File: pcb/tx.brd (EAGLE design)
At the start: 30 x 40 mm, 9 parts

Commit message: dt rx done
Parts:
- added BT1: (no value), SparkFun-Batteries:BATTCON_24.5MM_PTH
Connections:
- new net +: BT1.3
- new net -: BT1.2
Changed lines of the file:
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@@
 <?xml version="1.0" encoding="utf-8"?>
 <!DOCTYPE eagle SYSTEM "eagle.dtd">
-<eagle version="9.1.0">
+<eagle version="9.1.3">
 <drawing>
 <settings>
-<setting alwaysvectorfont="no"/>
+<setting alwaysvectorfont="yes"/>
 <setting verticaltext="up"/>
 </settings>
@@
 <element name="U$7" library="L1" package="M3_MOUNTING_HOLE_PACK" value="M3_MOUNTING_HOLE" x="2.54" y="2.54"/>
 <element name="U$8" library="L1" package="M3_MOUNTING_HOLE_PACK" value="M3_MOUNTING_HOLE" x="27.94" y="2.54"/>
+<element name="BT1" library="SparkFun-Batteries" package="BATTCON_24.5MM_PTH" value="" x="15.24" y="-12.7">
+<attribute name="SF_SKU" value="PRT-08863" x="15.24" y="-12.7" size="1.778" layer="27" display="off"/>
+</element>
 </elements>
 <signals>
@@
 <wire x1="14.2537" y1="29.8654" x2="15.7331" y2="29.8654" width="0" layer="19" extent="1-1"/>
 </signal>
+<signal name="-">
+<contactref element="BT1" pad="2"/>
+</signal>
+<signal name="+">
+<contactref element="BT1" pad="3"/>
+</signal>
 </signals>

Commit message: before tx firmware test
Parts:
- added C1, C3: 100nF, clock:0805
- added C10: 4.7µF, SparkFun-Passives:0805
- added C11, C12: 4.7uF, clock:0805
- added C2, C6: 2.2nF, clock:0805
- added C4: 1.5pF, clock:0805
- added C5: 1pF, clock:0805
- added C7: 4.7pF, clock:0805
- added C8, C9: 22pF, clock:0805
- added D1, D2: BAT20J, SparkFun-DiscreteSemi:SOD-323
- added L1: 3.9nH, basicBoard:0805
- added L2: 8.2nH, basicBoard:0805
- added L3: 2.7nH, basicBoard:0805
- added LED1: (no value), joyAnalog:CHIP-LED0805
- added R1: 22K, joyAnalog:0805
- added R2, R3: 5K1, joyAnalog:0805
- added R4: 4.7K, SparkFun-Passives:0805
- added R5: 27K, SparkFun-Passives:0805
- added S2: (no value), Adafruit Feather M0 Adalogger:SWITCH-SPST-SMD-A
- added U$9: XC6206_DEV, 3pos_slide_switch:SOT23R_INFINEON
- added U3: MCP73831T-2ACI/OT, microbuilder:SOT23-5
- added Y1: CRYSTAL-26MHZSMD-3.2X2.5, SparkFun-Clocks:CRYSTAL-SMD-3.2X2.5MM
- BT1: device SparkFun-Batteries:BATTCON_24.5MM_PTH -> tx:TX_SPARKFUN-BATTERIES_BATTCON_24.5MM_PTH
- U$1: value USBC_6P_DEV -> L1_USBC_6P_DEV; device L1:USBC_6P_PAC -> tx:L1_USBC_6P_PAC
- moved BT1 29.0 mm to (14.0, 16.3), flipped to the bottom, turned to 180 degrees
- moved U$6 5.60 mm to (26.4, 34.8)
- moved U$5 5.21 mm to (2.54, 34.4)
- moved U$4 5.00 mm to (10.3, 40.4)
- moved U$1 3.32 mm to (14.0, 3.30)
- moved U$3 2.18 mm to (13.5, 26.7), turned to 90 degrees
- moved U$2 1.93 mm to (14.5, 14.5), turned to 180 degrees
- moved U1 1.82 mm to (14.0, 21.5)
- moved U$8 1.80 mm to (26.1, 2.54)
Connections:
- removed net +: BT1.3
- removed net -: BT1.2
- removed net DVDD: U$3.19
- removed net VDD: U$3.15, U$3.18, U$3.7
- removed net VDD_PA: U$3.11
- removed net VSS: U$3.0, U$3.14, U$3.17, U$3.20, U$3.8
- new net +3V3: C1.1, C12.1, C2.1, U$3.15, U$3.18, U$3.7, U$9.2
- new net N$1: C3.1, U$3.19
- new net N$10: R3.1, U$1.CC2
- new net N$11: R2.1, U$1.CC1
- new net N$12: LED1.C, R4.1
- new net N$13: R4.2, U3.1
- new net N$14: U$3.4
- new net N$15: U$3.5
- new net N$16: U$3.3
- new net N$17: R5.1, U3.5
- new net N$19: D2.A, S2.2
- new net N$2: R1.1, U$3.16
- new net N$20: U$3.2
- new net N$21: U$3.1
- new net N$25: BT1.1, C10.1, S2.3, U3.3
- new net N$26: D1.A, U$1.VBUS1, U$1.VBUS2
- new net N$27: C11.1, D1.C, D2.C, LED1.A, U$9.3, U3.4
- new net N$3: L1.1, L2.1, U$3.13
- new net N$4: C4.1, L1.2
- new net N$5: C4.2, C5.1
- new net N$6: L2.2, L3.1, U$3.12
- new net N$7: C8.1, U$3.9, Y1.1
- new net N$8: C6.1, C7.1, L3.2, U$3.11
- new net N$9: C9.1, U$3.10, Y1.3
- net GND: now also BT1.2, C1.2, C10.2, C11.2, C12.2, C2.2, C3.2, C5.2, C6.2, C7.2, C8.2, C9.2, R1.2, R2.2, R3.2, R5.2, U$1.1, U$1.2, U$1.3, U$1.4, U$1.GND1, U$1.GND2, U$3.0, U$3.14, U$3.17, U$3.20, U$3.8, U$9.1, U3.2, Y1.2, Y1.4
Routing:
- added copper zone on layer 1, net GND
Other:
- board size 30 x 40 mm -> 28.1 x 45 mm

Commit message: tx before cleanup
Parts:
- added 4K7, R9: 22K, joyAnalog:0805
- added C13: 100nF, clock:0805
- added C14, C15: 4.7uF, clock:0805
- added JP1: (no value), adafruit_changed:1X03-CLEANBIG
- added LED2: (no value), joyAnalog:CHIP-LED0805
- added R10, R11: 100K, SparkFun-Passives:0805
- added R6, R7, R8: 27K, SparkFun-Passives:0805
- added U$10: 324_SW, 3pos_slide_switch:342_SWICH_FOOT
- added U$11: PINHD1X2, adafruit_changed:1X02
- S2: device Adafruit Feather M0 Adalogger:SWITCH-SPST-SMD-A -> tx:SWITCH-SPST-SMD-A
- moved C10 17.9 mm to (5.71, 1.65), turned to 270 degrees
- moved R2 11.6 mm to (24.6, 5.89), turned to 90 degrees
- moved U1 8.79 mm to (13.2, 12.8), turned to 270 degrees
- moved C1 7.66 mm to (8.20, 19.2)
- moved C2 7.66 mm to (8.20, 20.7)
- moved C3 7.66 mm to (8.20, 17.6)
- moved R1 7.66 mm to (8.20, 22.2)
- moved U$4 7.53 mm to (9.85, 32.9)
- moved C9 7.41 mm to (17.4, 23.1)
- moved Y1 7.37 mm to (17.4, 20.1)
- moved U$6 7.36 mm to (25.5, 27.5)
- moved U$3 7.22 mm to (12.8, 19.5)
- moved L2 7.20 mm to (13.1, 22.9)
- moved L1 7.19 mm to (12.4, 25.2)
- moved L3 7.19 mm to (14.0, 25.2)
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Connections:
- removed net AVDD: U1.11
- removed net AVDDVCSEL: U1.1
- removed net AVSSVCSEL: U1.2
- new net N$18: R6.1, U$2.18, U1.9
- new net N$22: R7.1, U$2.17, U1.10
- new net N$23: R8.1, U$2.2, U1.5
- new net N$24: U$2.3, U1.7
- new net N$28: 4K7.2, LED2.C
- new net N$29: LED2.A, U$2.7
- new net N$30: U$10.P$2, U$2.10
- new net N$31: JP1.3, U$2.19
- new net N$32: JP1.2, U$2.20
- new net N$33: JP1.1, U$2.8
- new net N$35: R10.1, R11.2, U$2.9
- net +3V3: now also C13.1, C14.1, C15.1, R6.2, R7.2, U$11.1, U$2.16, U$2.5, U1.1, U1.11
- net GND: now also 4K7.1, C13.2, C14.2, C15.2, R11.1, R8.2, R9.2, S2.G1, S2.G2, S2.G3, S2.G4, U$10.P$4, U$11.2, U$2.1, U$2.15, U$4.GND, U$4.GND@1, U1.2
- net N$14: now also U$2.13
- net N$15: now also U$2.12
- net N$16: now also U$2.11
- net N$20: now also U$2.14
- net N$21: now also R9.1, U$2.6
- net N$27: now also R10.2
- net N$5: now also U$4.FEED
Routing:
- net +3V3: track 0.00 -> 34.2 mm, vias 0 -> 8
- net N$35: track 0.00 -> 31.2 mm, vias 0 -> 2
- net N$30: track 0.00 -> 29.0 mm, vias 0 -> 2
- net GND: track 0.00 -> 26.1 mm
- net N$29: track 0.00 -> 25.9 mm, vias 0 -> 2
- net N$27: track 0.00 -> 21.3 mm
- net N$25: track 0.00 -> 21.2 mm
- net N$21: track 0.00 -> 20.9 mm, vias 0 -> 2
- net N$26: track 0.00 -> 18.1 mm
- net N$23: track 0.00 -> 13.9 mm, vias 0 -> 2
- net N$16: track 0.00 -> 13.4 mm, vias 0 -> 2
- net N$32: track 0.00 -> 13.3 mm, vias 0 -> 1
- net N$20: track 0.00 -> 12.5 mm
- net N$24: track 0.00 -> 11.6 mm, vias 0 -> 2
- net N$14: track 0.00 -> 10.6 mm
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- added copper zone on layer 16, net +3V3
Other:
- board size 28.1 x 45 mm -> 28 x 37 mm

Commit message: tx almost done
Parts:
- removed 4K7: 22K, joyAnalog:0805
- added R12: 4K7, joyAnalog:0805
- C14, C15: value 4.7uF -> 100nF
- R6, R7, R8: value 27K -> 10K
- R9: value 22K -> 10K
- moved U$10 2.39 mm to (1.68, 21.8)
- moved R8 0.94 mm to (11.6, 13.7)
- moved U1 0.86 mm to (14.0, 13.0)
- moved C13 0.76 mm to (13.9, 9.35)
- moved U$11 0.76 mm to (26.7, 23.4)
- moved JP1 0.71 mm to (26.7, 9.91)
- moved R6 0.69 mm to (16.4, 13.9)
- moved R7 0.66 mm to (16.4, 11.0)
- moved U$9 0.63 mm to (6.71, 14.9)
- moved C11 0.40 mm to (4.04, 15.7)
- moved C15 0.25 mm to (18.2, 8.59)
- moved C6 0.10 mm to (16.7, 28.1)
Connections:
- net GND: now also R12.1; no longer 4K7.1
- net N$28: now also R12.2; no longer 4K7.2
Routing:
- net GND: track 26.1 -> 23.8 mm
- net N$18: track 7.32 -> 6.40 mm
- net N$31: track 10.3 -> 11.1 mm
- net N$33: track 5.44 -> 6.20 mm
- net N$32: track 13.3 -> 14.0 mm
- net N$28: track 2.72 -> 2.00 mm
- net +3V3: track 34.2 -> 35.0 mm
- net N$22: track 8.23 -> 7.54 mm
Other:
- board text added: "-"
- board text added: "3V"
- board text added: "CHARGE"
- board text added: "CLK"
- board text added: "DIO"
- board text added: "GND"
- board text added: "OFF"
- board text added: "ON"
- board text added: "STAT"
- board text added: "TEST"
- board text added: "TX"
- board text added: "dayTripper TX dekuNukem 2018"
- board text added: "git.io/daytripper"

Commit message: cleanup
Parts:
- R12: value 4K7 -> 4.7K
- R2, R3: value 5K1 -> 5.1K
- R5: value 27K -> 22K
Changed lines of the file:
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@@
 <attribute name="PROD_ID" value="XTAL-12454" x="44.704" y="-0.4826" size="1.778" layer="27" rot="R90" display="off"/>
 </element>
-<element name="R3" library="joyAnalog" package="0805" value="5K1" x="22.8346" y="5.8928" smashed="yes" rot="R90">
+<element name="R3" library="joyAnalog" package="0805" value="5.1K" x="22.8346" y="5.8928" smashed="yes" rot="R90">
 <attribute name="NAME" x="23.4696" y="4.2799" size="0.8128" layer="25" rot="R180"/>
 </element>
-<element name="R2" library="joyAnalog" package="0805" value="5K1" x="24.5618" y="5.8928" smashed="yes" rot="R90">
+<element name="R2" library="joyAnalog" package="0805" value="5.1K" x="24.5618" y="5.8928" smashed="yes" rot="R90">
 <attribute name="NAME" x="26.1493" y="4.9022" size="0.8128" layer="25" rot="R90"/>
 </element>
@@
 <attribute name="NAME" x="3.0734" y="0.0889" size="0.8128" layer="25"/>
 </element>
-<element name="R5" library="SparkFun-Passives" package="0805" value="27K" x="10.0838" y="4.8514" smashed="yes" rot="R270">
+<element name="R5" library="SparkFun-Passives" package="0805" value="22K" x="10.0838" y="4.8514" smashed="yes" rot="R270">
 <attribute name="NAME" x="10.9093" y="5.6134" size="0.8128" layer="25" rot="R270"/>
 </element>
@@
 <attribute name="VALUE" x="7.874" y="22.606" size="1.27" layer="27" rot="R90"/>
 </element>
-<element name="R12" library="joyAnalog" package="0805" value="4K7" x="8.2296" y="24.9428" smashed="yes" rot="R180">
+<element name="R12" library="joyAnalog" package="0805" value="4.7K" x="8.2296" y="24.9428" smashed="yes" rot="R180">
 <attribute name="NAME" x="9.144" y="26.7081" size="0.8128" layer="25" rot="R180"/>
 <attribute name="VALUE" x="9.2456" y="26.3398" size="0.4064" layer="27" rot="R180"/>

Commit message: further cleanup
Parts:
- added SJ1, SJ2: JUMPER-SMT_2_NC_TRACE_NO-SILK, SparkFun-Jumpers:SMT-JUMPER_2_NC_TRACE_NO-SILK
- moved C14 1.22 mm to (21.6, 19.8)
- moved R9 0.98 mm to (24.2, 8.59)
- moved R12 0.41 mm to (8.23, 24.5)
- moved LED2 0.36 mm to (5.33, 23.5)
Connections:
- new net N$34: SJ2.2, U$2.3
- net +3V3: now also R8.2, SJ1.1, SJ2.1
- net GND: now also U$10.P$1; no longer R8.2
- net N$21: now also U$2.10; no longer U$2.6
- net N$23: now also SJ1.2; no longer R8.1, U1.5
- net N$24: now also R8.1, U1.5; no longer U$2.3, U1.7
- net N$29: now also U$2.9; no longer U$2.7
- net N$30: now also U$10.P$3, U$2.6; no longer U$2.10
- net N$35: now also U$2.7; no longer U$2.9
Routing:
- net N$34: track 0.00 -> 10.7 mm, vias 0 -> 1
- net N$24: track 11.9 -> 1.62 mm, vias 2 -> 0
- net N$35: track 31.2 -> 27.4 mm
- net +3V3: track 35.0 -> 37.5 mm
- net N$23: track 13.9 -> 12.0 mm, vias 2 -> 1
- net GND: track 23.8 -> 22.0 mm
- net N$29: track 25.9 -> 24.9 mm
- net N$30: track 28.9 -> 29.7 mm
- net N$33: track 6.20 -> 6.77 mm
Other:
- board text added: "0"
- board text added: "1"

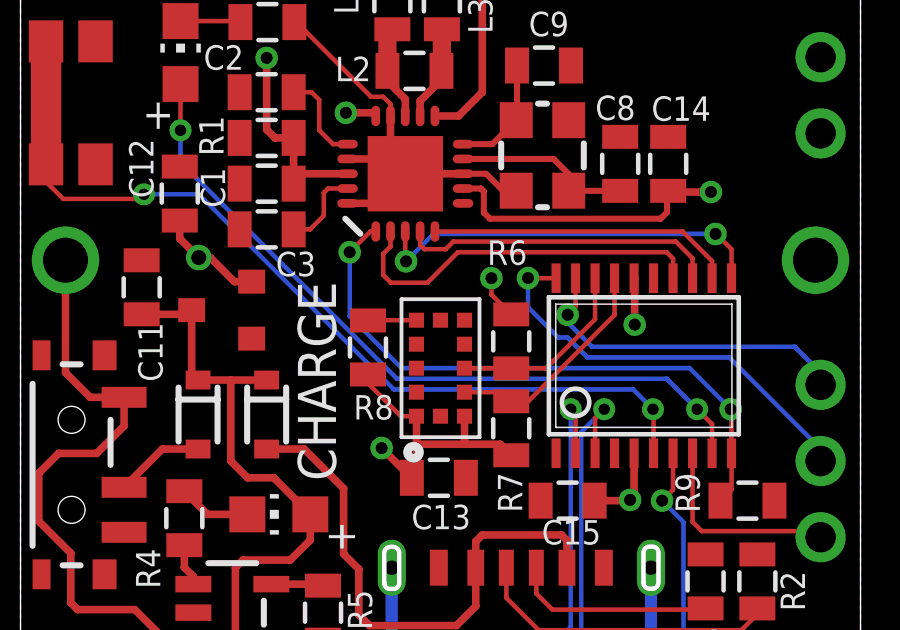
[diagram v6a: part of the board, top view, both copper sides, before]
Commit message: thinking about switch to tssop20
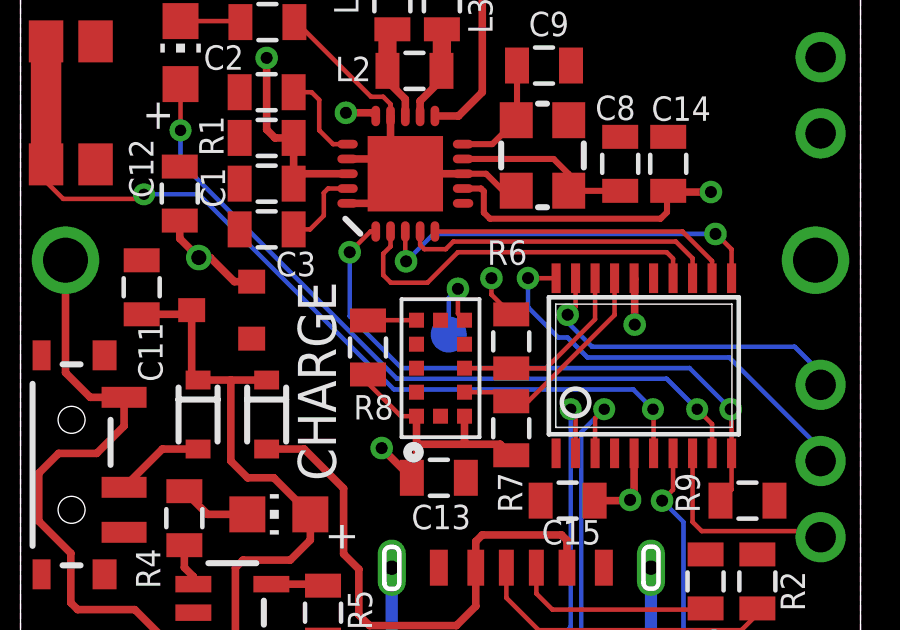
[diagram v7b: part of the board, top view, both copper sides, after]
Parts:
- added TP1: TPTP12R, testpad:TP12R
- C10: value 4.7µF -> 4.7uF
- R10, R11: value 100K -> 22K
- R12, R4: value 4.7K -> 5.1K
- R6, R7, R8, R9: value 10K -> 22K
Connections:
- new net N$36: TP1.TP, U1.7
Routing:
- net N$36: track 0.00 -> 2.79 mm, vias 0 -> 1
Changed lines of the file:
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@@
 <grid distance="2" unitdist="mil" unit="mil" style="lines" multiple="1" display="no" altdistance="5" altunitdist="mil" altunit="mil"/>
 <layers>
-<layer number="1" name="Top" color="4" fill="1" visible="no" active="yes"/>
+<layer number="1" name="Top" color="4" fill="1" visible="yes" active="yes"/>
 <layer number="2" name="Route2" color="16" fill="1" visible="no" active="no"/>
 <layer number="3" name="Route3" color="17" fill="1" visible="no" active="no"/>
@@
 <layer number="19" name="Unrouted" color="6" fill="1" visible="yes" active="yes"/>
 <layer number="20" name="Dimension" color="24" fill="1" visible="yes" active="yes"/>
-<layer number="21" name="tPlace" color="7" fill="1" visible="no" active="yes"/>
+<layer number="21" name="tPlace" color="7" fill="1" visible="yes" active="yes"/>
 <layer number="22" name="bPlace" color="7" fill="1" visible="yes" active="yes"/>
-<layer number="23" name="tOrigins" color="15" fill="1" visible="no" active="yes"/>
+<layer number="23" name="tOrigins" color="15" fill="1" visible="yes" active="yes"/>
 <layer number="24" name="bOrigins" color="15" fill="1" visible="yes" active="yes"/>
-<layer number="25" name="tNames" color="7" fill="1" visible="no" active="yes"/>
+<layer number="25" name="tNames" color="7" fill="1" visible="yes" active="yes"/>
 <layer number="26" name="bNames" color="7" fill="1" visible="yes" active="yes"/>
 <layer number="27" name="tValues" color="7" fill="1" visible="no" active="yes"/>
@@
 <layer number="37" name="tTest" color="7" fill="1" visible="no" active="yes"/>
 <layer number="38" name="bTest" color="7" fill="1" visible="no" active="yes"/>
-<layer number="39" name="tKeepout" color="4" fill="11" visible="no" active="yes"/>
+<layer number="39" name="tKeepout" color="4" fill="11" visible="yes" active="yes"/>
 <layer number="40" name="bKeepout" color="1" fill="11" visible="yes" active="yes"/>
-<layer number="41" name="tRestrict" color="4" fill="10" visible="no" active="yes"/>
+<layer number="41" name="tRestrict" color="4" fill="10" visible="yes" active="yes"/>
 <layer number="42" name="bRestrict" color="1" fill="10" visible="yes" active="yes"/>
 <layer number="43" name="vRestrict" color="2" fill="10" visible="no" active="yes"/>
@@
 <layer number="49" name="Reference" color="7" fill="1" visible="no" active="yes"/>
 <layer number="50" name="dxf" color="7" fill="1" visible="no" active="no"/>
-<layer number="51" name="tDocu" color="7" fill="1" visible="no" active="yes"/>
+<layer number="51" name="tDocu" color="7" fill="1" visible="yes" active="yes"/>
 <layer number="52" name="bDocu" color="7" fill="1" visible="yes" active="yes"/>
 <layer number="53" name="tGND_GNDA" color="7" fill="1" visible="no" active="no"/>
@@
 </element>
 <element name="U3" library="microbuilder" package="SOT23-5" value="MCP73831T-2ACI/OT" x="7.0612" y="4.8514" smashed="yes" rot="R270"/>
-<element name="R4" library="SparkFun-Passives" package="0805" value="4.7K" x="5.461" y="8.001" smashed="yes" rot="R270">
+<element name="R4" library="SparkFun-Passives" package="0805" value="5.1K" x="5.461" y="8.001" smashed="yes" rot="R270">
 <attribute name="NAME" x="3.8481" y="6.985" size="0.8128" layer="25" rot="R270"/>
 </element>
-<element name="C10" library="SparkFun-Passives" package="0805" value="4.7µF" x="5.715" y="1.651" smashed="yes" rot="R270">
+<element name="C10" library="SparkFun-Passives" package="0805" value="4.7uF" x="5.715" y="1.651" smashed="yes" rot="R270">
 <attribute name="NAME" x="4.9403" y="0.127" size="0.8128" layer="25" rot="R90"/>
 </element>
@@
 <attribute name="VALUE" x="9.8806" y="10.668" size="1.27" layer="27" rot="R180"/>
 </element>
-<element name="R6" library="SparkFun-Passives" package="0805" value="10K" x="16.3576" y="13.8938" smashed="yes" rot="R90">
+<element name="R6" library="SparkFun-Passives" package="0805" value="22K" x="16.3576" y="13.8938" smashed="yes" rot="R90">
 <attribute name="NAME" x="16.891" y="17.2593" size="0.8128" layer="25" rot="R180"/>
 </element>
-<element name="R7" library="SparkFun-Passives" package="0805" value="10K" x="16.3576" y="10.9982" smashed="yes" rot="R270">
+<element name="R7" library="SparkFun-Passives" package="0805" value="22K" x="16.3576" y="10.9982" smashed="yes" rot="R270">
 <attribute name="NAME" x="15.9131" y="9.525" size="0.8128" layer="25" rot="R270"/>
 </element>
-<element name="R8" library="SparkFun-Passives" package="0805" value="10K" x="11.5824" y="13.6906" smashed="yes" rot="R270">
+<element name="R8" library="SparkFun-Passives" package="0805" value="22K" x="11.5824" y="13.6906" smashed="yes" rot="R270">
 <attribute name="NAME" x="11.0998" y="11.2903" size="0.8128" layer="25"/>
 </element>
@@
 </element>
 <element name="U$10" library="3pos_slide_switch" package="342_SWICH_FOOT" value="324_SW" x="1.6764" y="21.844" smashed="yes" rot="R90"/>
-<element name="R9" library="joyAnalog" package="0805" value="10K" x="24.2316" y="8.5852" smashed="yes">
+<element name="R9" library="joyAnalog" package="0805" value="22K" x="24.2316" y="8.5852" smashed="yes">
 <attribute name="NAME" x="22.6441" y="8.1788" size="0.8128" layer="25" rot="R90"/>
 </element>
@@
 <attribute name="VALUE" x="7.874" y="22.2504" size="1.27" layer="27" rot="R90"/>
 </element>
-<element name="R12" library="joyAnalog" package="0805" value="4.7K" x="8.2296" y="24.5364" smashed="yes" rot="R180">
+<element name="R12" library="joyAnalog" package="0805" value="5.1K" x="8.2296" y="24.5364" smashed="yes" rot="R180">
 <attribute name="NAME" x="9.144" y="26.3017" size="0.8128" layer="25" rot="R180"/>
 <attribute name="VALUE" x="9.2456" y="25.9334" size="0.4064" layer="27" rot="R180"/>
@@
 </element>
 <element name="U$11" library="adafruit_changed" package="1X02" value="PINHD1X2" x="26.67" y="23.368" smashed="yes" rot="R90"/>
-<element name="R10" library="SparkFun-Passives" package="0805" value="100K" x="8.8392" y="1.651" smashed="yes" rot="R90">
+<element name="R10" library="SparkFun-Passives" package="0805" value="22K" x="8.8392" y="1.651" smashed="yes" rot="R90">
 <attribute name="NAME" x="6.9723" y="3.0226" size="0.8128" layer="25" rot="R270"/>
 <attribute name="VALUE" x="10.2362" y="0.635" size="0.4064" layer="27" rot="R90"/>
 </element>
-<element name="R11" library="SparkFun-Passives" package="0805" value="100K" x="10.4648" y="1.651" smashed="yes" rot="R270">
+<element name="R11" library="SparkFun-Passives" package="0805" value="22K" x="10.4648" y="1.651" smashed="yes" rot="R270">
 <attribute name="NAME" x="12.0269" y="0.127" size="0.8128" layer="25" rot="R90"/>
 <attribute name="VALUE" x="9.0678" y="2.667" size="0.4064" layer="27" rot="R270"/>
@@
 <element name="SJ2" library="SparkFun-Jumpers" package="SMT-JUMPER_2_NC_TRACE_NO-SILK" value="JUMPER-SMT_2_NC_TRACE_NO-SILK" x="17.78" y="2.7432" smashed="yes" rot="MR90">
 <attribute name="VALUE" x="16.637" y="2.7432" size="0.6096" layer="28" font="vector" ratio="20" rot="MR90" align="top-center"/>
+</element>
+<element name="TP1" library="testpad" library_urn="urn:adsk.eagle:library:385" package="TP12R" package3d_urn="urn:adsk.eagle:package:27963/1" value="TPTP12R" x="14.2748" y="14.1224" smashed="yes" rot="MR0">
+<attribute name="TP_SIGNAL_NAME" value="" x="14.2748" y="11.5824" size="1" layer="38" rot="MR0"/>
+<attribute name="VALUE" x="14.7828" y="13.4874" size="0.0254" layer="28" rot="MR0"/>
 </element>
 </elements>
@@
 <wire x1="9.1948" y1="24.5364" x2="9.1296" y2="24.5364" width="0.1524" layer="1"/>
 <contactref element="U$10" pad="P$1"/>
+<wire x1="0.7018" y1="6.129" x2="2.8018" y2="6.129" width="0" layer="19" extent="1-1"/>
 <wire x1="0.7018" y1="13.429" x2="2.8018" y2="13.429" width="0" layer="19" extent="1-1"/>
-<wire x1="0.7018" y1="6.129" x2="2.8018" y2="6.129" width="0" layer="19" extent="1-1"/>
 </signal>
 <signal name="+3V3">
@@
 <wire x1="0.8514" y1="23.894" x2="0.8514" y2="19.794" width="1.016" layer="1"/>
 </signal>
+<signal name="N$36">
+<contactref element="U1" pad="7"/>
+<contactref element="TP1" pad="TP"/>
+<wire x1="14.8" y1="14.6" x2="14.5796" y2="14.8204" width="0.1524" layer="1"/>
+<wire x1="14.5796" y1="14.8204" x2="14.5796" y2="15.6464" width="0.1524" layer="1"/>
+<via x="14.5796" y="15.6464" extent="1-16" drill="0.4"/>
+<wire x1="14.5796" y1="15.6464" x2="14.2748" y2="15.3416" width="0.1524" layer="16"/>
+<wire x1="14.2748" y1="15.3416" x2="14.2748" y2="14.1224" width="0.1524" layer="16"/>
+</signal>
 </signals>
 <mfgpreviewcolors>
@@
 which will not be processed correctly with this version.
 </note>
+<note version="8.2" severity="warning">
+Since Version 8.2, EAGLE supports online libraries. The ids
+of those online libraries will not be understood (or retained)
+with this version.
+</note>
+<note version="8.3" severity="warning">
+Since Version 8.3, EAGLE supports URNs for individual library
+assets (packages, symbols, and devices). The URNs of those assets
+will not be understood (or retained) with this version.
+</note>
+<note version="8.3" severity="warning">
+Since Version 8.3, EAGLE supports the association of 3D packages
+with devices in libraries, schematics, and board files. Those 3D
+packages will not be understood (or retained) with this version.
+</note>
 </compatibility>
